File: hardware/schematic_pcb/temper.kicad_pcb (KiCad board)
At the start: 2 copper layers, 63 x 91 mm, 52 parts, among them J1 conn_01x03, J10 conn_01x05, J11 Conn_01x10, J12 2.54mm Plugin Gold 7P Brass S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, J2 conn_01x03, J3 conn_01x03, J4 conn_01x03, J5 Charge Connector, J6 Conn_01x20, J7 Conn_01x20, J8 conn_01x05, J9 conn_01x05, M1 DMP3099L-7, M2 DMP3099L-7, Q1 2N7002, SW1 Factory Reset, SW2 Reset, SW3 ON/OFF, U1 SPI ROTARY ENCODER, U2 MCP9700, U3 Pico_W, U4 TL431DBZ

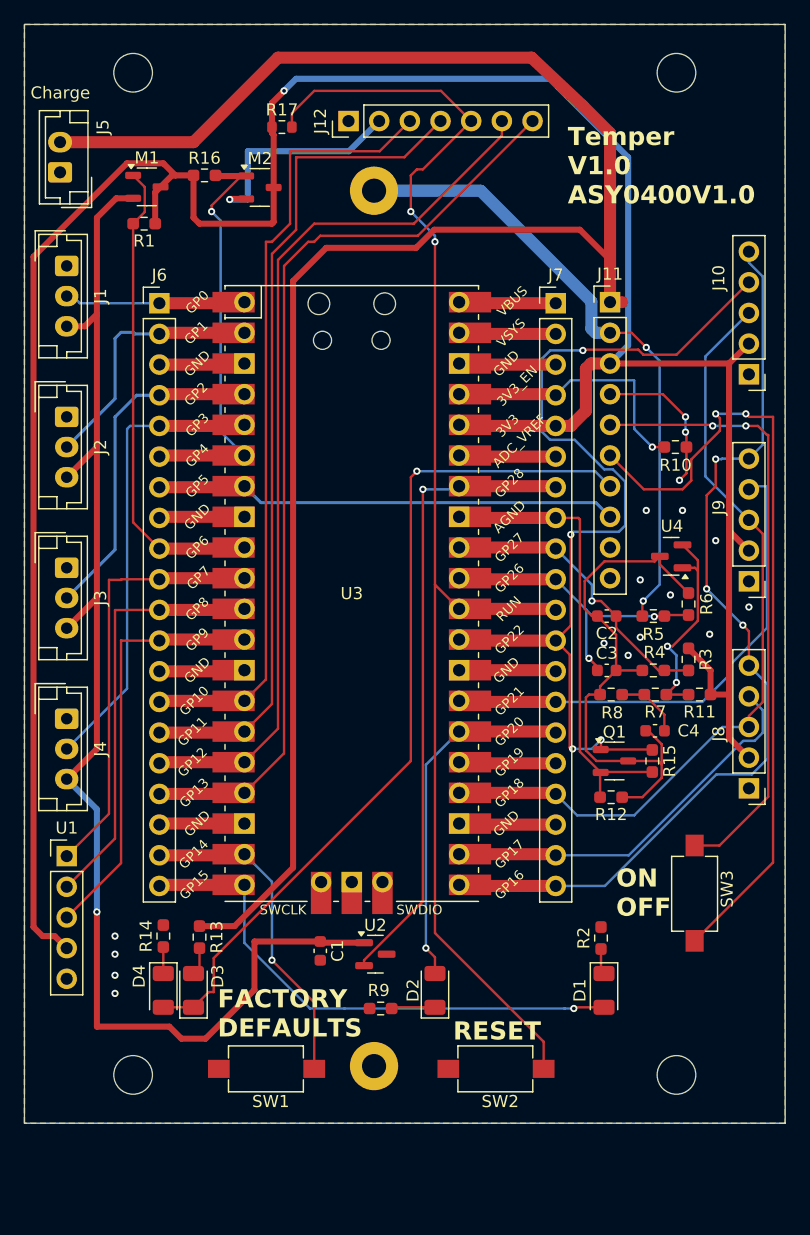
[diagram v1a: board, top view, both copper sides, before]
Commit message: V1.2 using an ESP32 rather than a RPi Pico W. The ESP32 can handle low power modes better than the RPi Pico W.
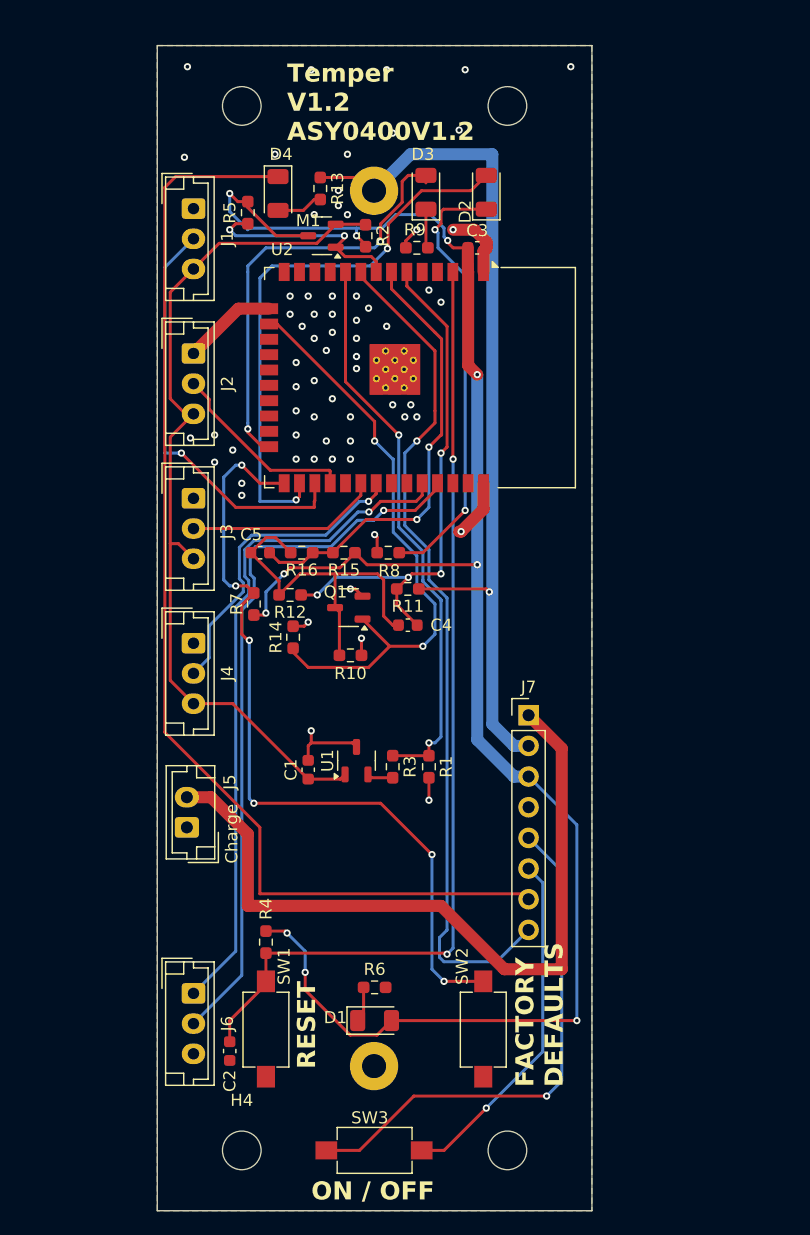
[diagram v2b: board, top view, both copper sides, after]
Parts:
- removed J10, J8, J9: conn_01x05, Connector_PinHeader_2.54mm:PinHeader_1x05_P2.54mm_Vertical
- removed J11: Conn_01x10, Connector_PinHeader_2.54mm:PinHeader_1x10_P2.54mm_Vertical
- removed J12: 2.54mm Plugin Gold 7P Brass Straight 1x7P Plugin,P=2.54mm F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, Connector_PinHeader_2.54mm:PinHeader_1x07_P2.54mm_Vertical
- removed M2: DMP3099L-7, Package_TO_SOT_SMD:SOT-23-3
- removed MH1, MH2, MH3, MH4: MountingHole_3.2mm_M3, MountingHole:MountingHole_3.2mm_M3
- removed R17: 10k, Resistor_SMD:R_0603_1608Metric
- removed U3: Pico_W, PJA_RP_pico:RPi_Pico_SMD_TH
- removed U4: TL431DBZ, Package_TO_SOT_SMD:SOT-23
- added C5: 0.1uf, Capacitor_SMD:C_0603_1608Metric, F.Cu at (138.5, 94.8)
- added H1: MountingHole_3.2mm_M3, MountingHole:MountingHole_3.2mm_M3, F.Cu at (137.0, 57.8)
- added H2: MountingHole_3.2mm_M3, MountingHole:MountingHole_3.2mm_M3, F.Cu at (159.0, 57.8)
- added H3: MountingHole_3.2mm_M3, MountingHole:MountingHole_3.2mm_M3, F.Cu at (159.0, 144.2)
- added H4: MountingHole_3.2mm_M3, MountingHole:MountingHole_3.2mm_M3, F.Cu at (137.0, 144.2)
- D1: value Blue Bluetooth LED -> PWR LED
- D2: value Green WiFi LED -> Blue Bluetooth LED
- D3: value Red Charging LED -> Green WiFi LED
- D4: value Greeen Charged LED -> Red Charging LED
- J6: value Conn_01x20 -> MCU Serial I/F; footprint Connector_PinHeader_2.54mm:PinHeader_1x20_P2.54mm_Vertical -> Connector_JST:JST_EH_B3B-EH-A_1x03_P2.50mm_Vertical
- J7: value Conn_01x20 -> Conn_01x08; footprint Connector_PinHeader_2.54mm:PinHeader_1x20_P2.54mm_Vertical -> Connector_PinHeader_2.54mm:PinHeader_1x08_P2.54mm_Vertical
- R1: value 100k -> 12k
- R10: value 10k -> DNF
- R11: value 680R -> 150k
- R12: value DNF -> 47k
- R14: value 470R -> 100k
- R15: value 100k -> 150k
- R16: value 100k -> 68k
- R2: value 470R -> DNF
- R3: value 120k -> 22k
- R4: value 68k -> 10k
- R5: value 120k -> 100k
- R6: value 47k -> 470R
- R7: value 100k -> 10k
- R8: value 100k -> 470R
- SW1: value Factory Reset -> Reset
- SW2: value Reset -> Factory Reset
- U1: value SPI ROTARY ENCODER -> MCP9700; footprint Connector_PinHeader_2.54mm:PinHeader_1x05_P2.54mm_Vertical -> Package_TO_SOT_SMD:SOT-23-3
- U2: value MCP9700 -> ESP32-WROOM-32; footprint Package_TO_SOT_SMD:SOT-23 -> PJA_ESP32-footprints-Lib:ESP32-WROOM-32
- moved D3 68.8 mm to (152.2, 64.9)
- moved D4 66.7 mm to (140.0, 65.0)
- moved D2 66.2 mm to (157.2, 64.9)
- moved R9 63.1 mm to (151.5, 69.5)
- moved R13 62.8 mm to (143.5, 64.6)
- moved R2 61.3 mm to (147.2, 68.5), turned to -90 degrees
- moved J6 57.2 mm to (133.0, 131.2), turned to -90 degrees
- moved J5 55.3 mm to (132.4, 117.5)
- moved R1 50.8 mm to (152.5, 112.5), turned to -90 degrees
- moved U2 47.8 mm to (148.8, 80.2), turned to -90 degrees
- moved C2 47.7 mm to (136.0, 136.0), turned to -90 degrees
- moved R5 47.4 mm to (137.5, 66.6), turned to -90 degrees
- moved R6 41.0 mm to (148.0, 130.8), turned to 0 degrees
- moved R4 39.2 mm to (139.0, 127.0), turned to -90 degrees
- moved C3 36.6 mm to (156.5, 69.5)
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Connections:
- C2 pad 1: Net-(J7-Pin_9) -> Net-(SW1-B)
- C2 pad 2: Net-(Q1-D) -> GND
- C3 pad 1: Net-(J7-Pin_10) -> 3v3
- C3 pad 2: Net-(Q1-D) -> GND
- C4 pad 1: /1.25V_REF -> Net-(U2-IO34)
- D1 pad 2: Net-(D1-A) -> 3v3
- D4 pad 2: Net-(D3-K) -> Net-(D4-A)
- J6 pad 1: /DHT22_1 -> /RXD
- J6 pad 2: /DHT22_2 -> /TXD
- J6 pad 3: Net-(J6-Pin_3) -> GND
- J7 pad 1: Net-(J7-Pin_1) -> +5v
- J7 pad 2: Net-(J7-Pin_2) -> /+VBAT
- J7 pad 3: Net-(J7-Pin_3) -> 3v3
- J7 pad 4: Net-(J7-Pin_4) -> GND
- J7 pad 5: 3v3 -> Net-(J7-Pin_5)
- J7 pad 7: /GPI28_ADC2 -> Net-(D4-K)
- J7 pad 8: Net-(J7-Pin_8) -> //PWR_CYCLE
- M1 pad 1: //DHT22_ON -> //TON
- Q1 pad 1: /GPIO22 -> Net-(Q1-G)
- Q1 pad 2: Net-(J7-Pin_8) -> GND
- R1 pad 1: 3v3 -> /BRD_TEMP
- R1 pad 2: //DHT22_ON -> GND
- R10 pad 1: Net-(J7-Pin_4) -> Net-(Q1-D)
- R11 pad 1: 3v3 -> /+VBAT
- R11 pad 2: /2.5V_REF -> Net-(U2-IO34)
- R12 pad 1: Net-(Q1-D) -> Net-(U2-IO34)
- R12 pad 2: Net-(J7-Pin_8) -> Net-(Q1-D)
- R13 pad 1: +5v -> /+VBAT
- R13 pad 2: Net-(D3-A) -> Net-(D4-A)
- R14 pad 1: Net-(D4-K) -> Net-(Q1-G)
- R15 pad 1: /GPIO22 -> 3v3
- R15 pad 2: Net-(J7-Pin_8) -> Net-(U2-IO35)
- R16 pad 1: 3v3 -> Net-(U2-IO35)
- R16 pad 2: //DISP_ON -> Net-(Q1-D)
- R2 pad 1: Net-(D1-K) -> Net-(J1-Pin_3)
- R2 pad 2: GND -> 3v3
- R3 pad 1: 3v3 -> /BRD_TEMP
- R3 pad 2: Net-(J7-Pin_9) -> Net-(U1-VOUT)
- R4 pad 1: Net-(J7-Pin_9) -> 3v3
- R4 pad 2: Net-(Q1-D) -> Net-(SW1-B)
- R5 pad 1: /+VBAT -> 3v3
- R5 pad 2: Net-(J7-Pin_10) -> //TON
- R6 pad 1: Net-(J7-Pin_10) -> Net-(D1-K)
- R6 pad 2: Net-(Q1-D) -> GND
- R7 pad 1: /2.5V_REF -> 3v3
- R7 pad 2: /1.25V_REF -> Net-(SW2-B)
- R8 pad 1: /1.25V_REF -> Net-(D2-K)
- R8 pad 2: Net-(Q1-D) -> GND
- R9 pad 1: Net-(D2-K) -> Net-(D3-K)
- SW1 pad 2: Net-(J6-Pin_19) -> Net-(SW1-B)
- SW2 pad 2: /RUN -> Net-(SW2-B)
- SW3 pad 1: Net-(J11-Pin_6) -> Net-(J7-Pin_6)
- SW3 pad 2: Net-(J11-Pin_5) -> Net-(J7-Pin_5)
- U1 pad 1: /ROTARY_ENC_CLK -> Net-(J1-Pin_3)
- U1 pad 2: /ROTARY_ENC_DATA -> Net-(U1-VOUT)
- U1 pad 3: /ROTARY_ENC_SW -> GND
- U2 pad 1: Net-(J1-Pin_3) -> GND
- U2 pad 2: /GPI28_ADC2 -> 3v3
- U2 pad 3: GND -> Net-(SW1-B)
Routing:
- net /RUN: track 114.1 -> 0.00 mm, vias 2 -> 0
- net +5v: track 156.9 -> 62.6 mm
- net Net-(D4-K): track 2.19 -> 93.9 mm
- net Net-(SW1-B): track 0.00 -> 80.3 mm, vias 0 -> 2
- net /GPIO16: track 78.0 -> 0.00 mm, vias 3 -> 0
- net /GPIO22: track 78.0 -> 0.00 mm, vias 4 -> 0
- net /GPIO13: track 77.6 -> 0.00 mm
- net /GPIO12: track 73.8 -> 0.00 mm
- net /GPIO11: track 69.6 -> 0.00 mm
- net Net-(D3-K): track 71.3 -> 3.27 mm, vias 1 -> 0
- net Net-(SW2-B): track 0.00 -> 66.5 mm, vias 0 -> 6
- net /GPIO18: track 66.0 -> 0.00 mm
- net Net-(J11-Pin_6): track 65.8 -> 0.00 mm, vias 2 -> 0
- net 3v3: track 222.4 -> 156.7 mm, vias 1 -> 10
- net /GPIO10: track 65.4 -> 0.00 mm
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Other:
- board size 63 x 91 mm -> 36 x 96.5 mm
- board text added: "ON / OFF"
- board text added: "Temper V1.2 ASY0400V1.2"
- board text removed: "ON OFF"
- board text removed: "Temper V1.0 ASY0400V1.0"

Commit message: - Move ADC2 pins as ADC2 cannot be used with WiFi. - Add power up reset controller to ensure MCU boots after powercyle event.
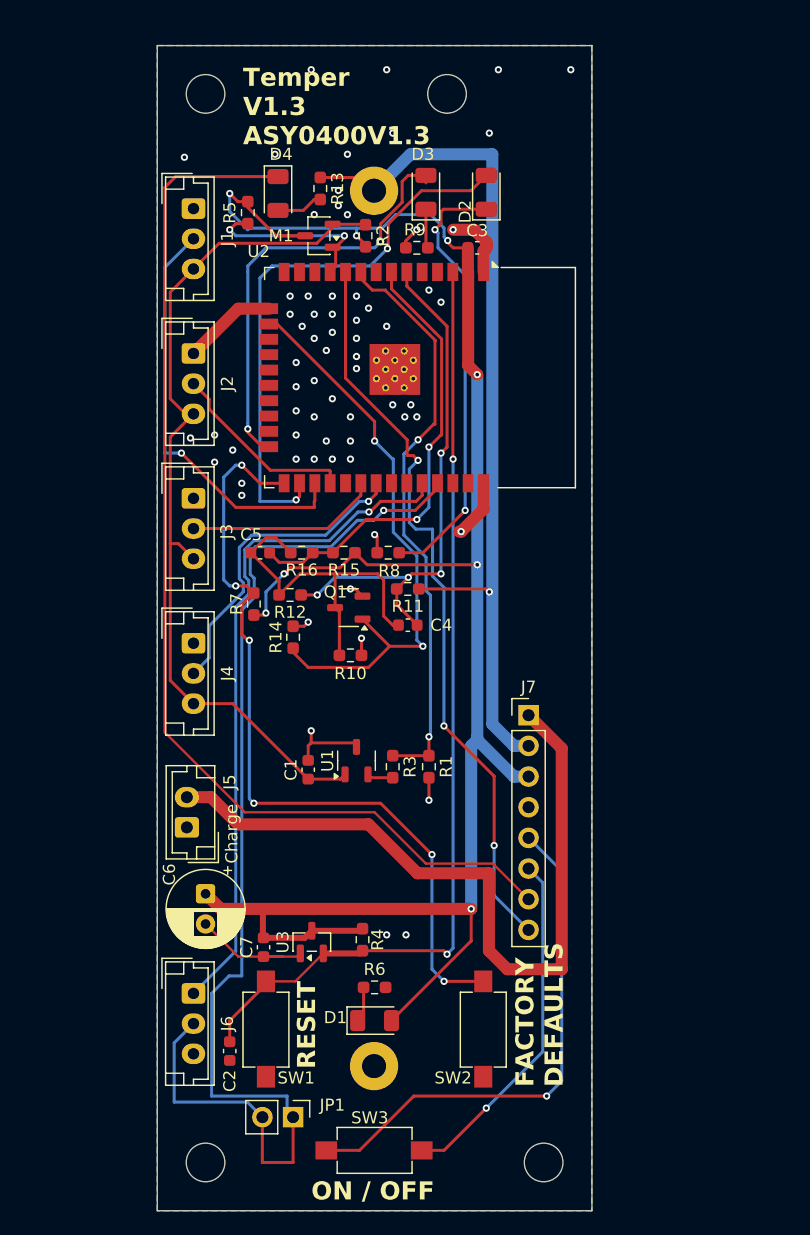
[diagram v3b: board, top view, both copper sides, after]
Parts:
- removed H1, H2, H3, H4: MountingHole_3.2mm_M3, MountingHole:MountingHole_3.2mm_M3
- added C6: 470uf, Capacitor_THT:CP_Radial_D6.3mm_P2.50mm, F.Cu at (134.0, 123.0)
- added C7: 0.1uf, Capacitor_SMD:C_0603_1608Metric, F.Cu at (138.8, 127.4)
- added JP1: Jumper_2_Open, Connector_PinHeader_2.54mm:PinHeader_1x02_P2.54mm_Vertical, F.Cu at (141.2, 141.5)
- added MH1: MountingHole_3.2mm_M3, MountingHole:MountingHole_3.2mm_M3, F.Cu at (134.0, 56.8)
- added MH2: MountingHole_3.2mm_M3, MountingHole:MountingHole_3.2mm_M3, F.Cu at (154.0, 56.8)
- added MH3: MountingHole_3.2mm_M3, MountingHole:MountingHole_3.2mm_M3, F.Cu at (162.0, 145.2)
- added MH4: MountingHole_3.2mm_M3, MountingHole:MountingHole_3.2mm_M3, F.Cu at (134.0, 145.2)
- added U3: APX803-31SAG-7, Package_TO_SOT_SMD:SOT-23, F.Cu at (142.8, 127.0)
- R1: value 12k -> DNF
- R3: value 22k -> 0R
- moved R4 8.00 mm to (147.0, 126.8)
- moved M1 0.25 mm to (143.4, 68.5)
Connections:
- net Net-(SW1-B) renamed //RESET
- J7 pad 8: //PWR_CYCLE -> /PWR_CYCLE
- U2 pad 10: /BRD_TEMP -> /PWR_CYCLE
- U2 pad 11: unconnected-(U2-IO26-Pad11) -> //TON
- U2 pad 8: //TON -> unconnected-(U2-IO32-Pad8)
- U2 pad 9: //PWR_CYCLE -> /BRD_TEMP
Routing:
- net //PWR_CYCLE: track 70.7 -> 0.00 mm, vias 1 -> 0
- net /PWR_CYCLE: track 0.00 -> 62.5 mm, vias 0 -> 3
- net /TXD: track 59.4 -> 98.6 mm
- net GND: track 34.5 -> 44.7 mm, vias 66 -> 67
- net 3v3: track 156.7 -> 162.8 mm, vias 10 -> 8
- net Net-(D4-K): track 93.9 -> 91.4 mm
- net //TON: track 17.4 -> 14.9 mm
- net /BRD_TEMP: track 47.1 -> 48.4 mm
- net //RESET: track 80.3 -> 79.1 mm
- net Net-(Q1-G): track 48.7 -> 47.9 mm
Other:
- board text added: "Temper V1.3 ASY0400V1.3"
- board text removed: "Temper V1.2 ASY0400V1.2"

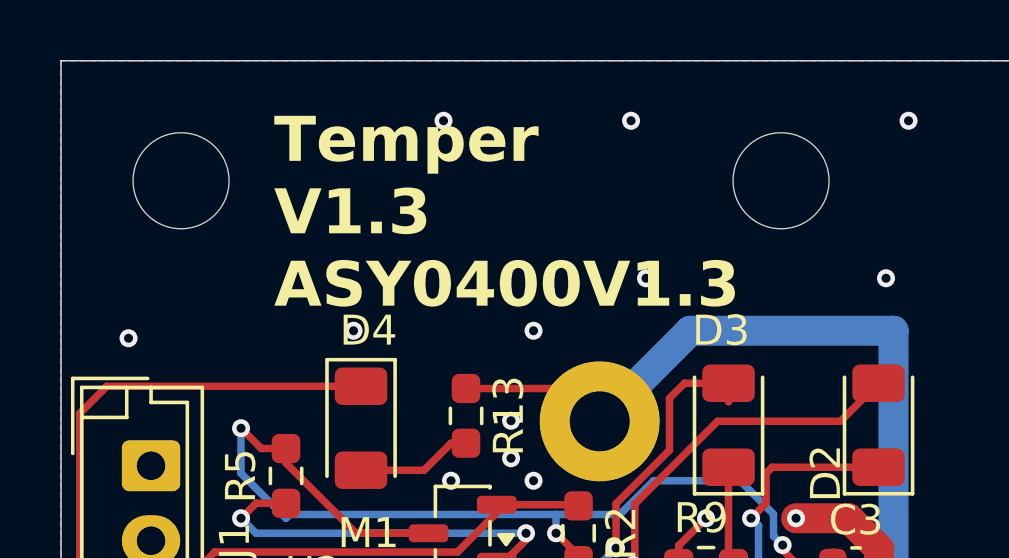
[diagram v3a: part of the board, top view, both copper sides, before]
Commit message: Bump PCB to V1.4 to accept the 26700 Sodium ION battery.
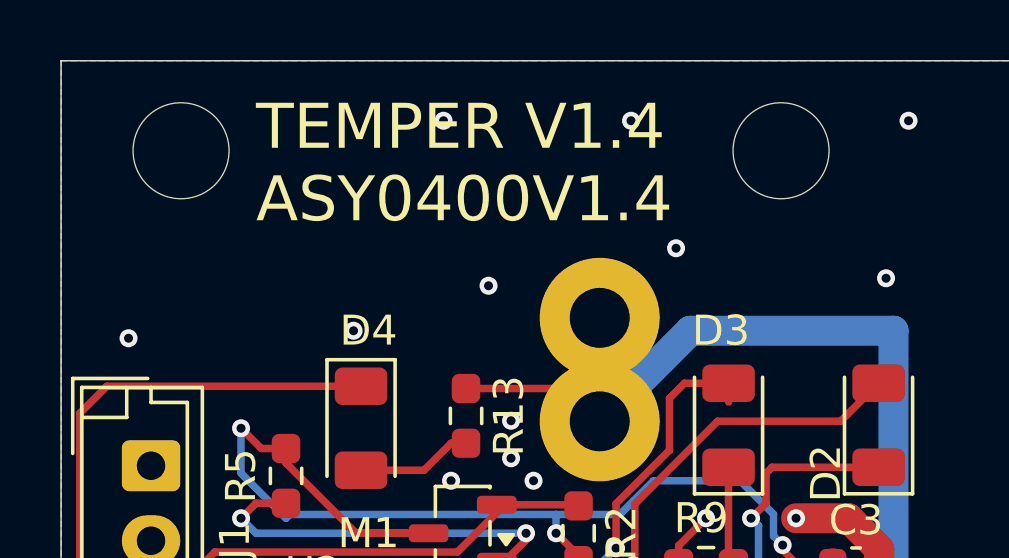
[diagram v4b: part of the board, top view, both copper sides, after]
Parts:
- BT1: footprint PJA_Connectors:18650_battery_holder -> PJA_Connectors:18650_26700_battery_holder
- moved MH1 1.00 mm to (134.0, 55.8)
- moved MH2 1.00 mm to (154.0, 55.8)
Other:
- board text added: "TEMPER V1.4 ASY0400V1.4"
- board text removed: "Temper V1.3 ASY0400V1.3"
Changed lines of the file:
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@@
 	(title_block
 		(title "Temper (temperature monitoring device).")
-		(date "2025-10-06")
-		(rev "1.3")
+		(date "2025-10-13")
+		(rev "1.4")
 	)
 	(layers
@@
 	(footprint "MountingHole:MountingHole_3.2mm_M3"
 		(layer "F.Cu")
-		(at 154 56.75)
+		(at 154 55.75)
 		(descr "Mounting Hole 3.2mm, M3, no annular, generated by kicad-footprint-generator mountinghole.py")
 		(tags "mountinghole M3")
@@
 	(footprint "MountingHole:MountingHole_3.2mm_M3"
 		(layer "F.Cu")
-		(at 134 56.75)
+		(at 134 55.75)
 		(descr "Mounting Hole 3.2mm, M3, no annular, generated by kicad-footprint-generator mountinghole.py")
 		(tags "mountinghole M3")
@@
 		)
 	)
-	(footprint "PJA_Connectors:18650_battery_holder"
+	(footprint "PJA_Connectors:18650_26700_battery_holder"
 		(layer "F.Cu")
 		(at 147.955 101.02 -90)
@@
 		(attr smd)
 		(fp_line
-			(start -38.608 10.668)
-			(end -38.608 -10.668)
+			(start 38.8 10.668)
+			(end -42.4 10.668)
 			(stroke
 				(width 0.12)
@@
 		)
 		(fp_line
-			(start 38.608 10.668)
-			(end -38.608 10.668)
+			(start -42.4 10.636)
+			(end -42.4 -10.7)
 			(stroke
 				(width 0.12)
@@
 		)
 		(fp_line
-			(start -38.608 -10.668)
-			(end 38.608 -10.668)
+			(start 38.8 -10.484)
+			(end 38.8 10.6)
 			(stroke
 				(width 0.12)
@@
 		)
 		(fp_line
-			(start 38.608 -10.668)
-			(end 38.608 10.668)
+			(start -42.4 -10.668)
+			(end 38.8 -10.668)
 			(stroke
 				(width 0.12)
@@
 			(layer "B.SilkS")
 		)
-		(fp_text user "BAT +VE"
-			(at -32.02 3.955 270)
+		(fp_text user "-VE"
+			(at 37.25 4 270)
 			(unlocked yes)
 			(layer "B.SilkS")
@@
 			)
 		)
-		(fp_text user "GND"
-			(at 37.25 4 270)
+		(fp_text user "18650/26700 Battery Holder"
+			(at 9.25 4.25 270)
 			(unlocked yes)
 			(layer "B.SilkS")
@@
 			)
 		)
-		(fp_text user "18650 LION Battery Holder"
-			(at 5.48 -11.545 270)
+		(fp_text user "+VE"
+			(at -34.75 4 270)
 			(unlocked yes)
 			(layer "B.SilkS")
@@
 		)
 		(pad "1" thru_hole circle
+			(at -39.7 0 270)
+			(size 4 4)
+			(drill 2)
+			(layers "*.Cu" "*.Mask")
+			(remove_unused_layers no)
+			(net 1 "/+VBAT")
+			(pinfunction "+")
+			(pintype "passive")
+		)
+		(pad "1" thru_hole circle
 			(at -36.25 0 270)
 			(size 4 4)
@@
 		)
 	)
-	(gr_text "FACTORY\nDEFAULTS"
-		(at 163.75 139 90)
+	(gr_text "TEMPER V1.4\nASY0400V1.4"
+		(at 136.5 58.25 0)
 		(layer "F.SilkS")
 		(effects
 			(font
 				(size 1.5 1.5)
-				(thickness 0.3)
-				(bold yes)
+				(thickness 0.15)
 			)
 			(justify left bottom)
 		)
 	)
-	(gr_text "Temper\nV1.3\nASY0400V1.3"
-		(at 137.1 61.1 0)
+	(gr_text "FACTORY\nDEFAULTS"
+		(at 163.75 139 90)
 		(layer "F.SilkS")
 		(effects
@@
 		(layer "F.Fab")
 		(pts
-			(xy 123.25 145.25) (xy 123.25 56.75)
+			(xy 123.25 145.25) (xy 123.25 55.75)
 		)
 		(height 0)
@@
 			(keep_text_aligned yes)
 		)
-		(gr_text "88.5000 mm"
-			(at 122.1 101 90)
+		(gr_text "89.5000 mm"
+			(at 122.1 100.5 90)
 			(layer "F.Fab")
 			(effects
@@
 		(layer "F.Fab")
 		(pts
-			(xy 134 56.75) (xy 134 52.75)
+			(xy 134 55.75) (xy 134 52.75)
 		)
 		(height -10.75)
@@
 			(keep_text_aligned yes)
 		)
-		(gr_text "4.0000 mm"
-			(at 122.1 54.75 90)
+		(gr_text "3.0000 mm"
+			(at 122.1 54.25 90)
 			(layer "F.Fab")
 			(effects
@@
 	)
 	(via
-		(at 149.5 60)
+		(at 150.5 59)
 		(size 0.6)
 		(drill 0.3)
@@
 	)
 	(via
-		(at 145.75 61.75)
+		(at 144.25 60.25)
 		(size 0.6)
 		(drill 0.3)
